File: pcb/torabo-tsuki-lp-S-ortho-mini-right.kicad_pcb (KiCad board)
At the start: 2 copper layers, 138.8 x 69 mm, 67 parts, among them J201 Conn_01x06_MountingPin, SW201 SW_SPDT, SW43 SW_Push, SW44 SW_Push, SW45 SW_Push, SW46 SW_Push, SW47 SW_Push, SW48 SW_Push, SW50 SW_Push, SW51 SW_Push, SW52 SW_Push, SW53 SW_Push, SW54 SW_Push, SW55 SW_Push, SW57 SW_Push, SW58 SW_Push, SW59 SW_Push, SW60 SW_Push, SW61 SW_Push, SW62 SW_Push, SW63 SW_Push, SW64 SW_Push, SW65 SW_Push, SW69 SW_Push, SW70 SW_Push, U201 XIAO nRF52840 Plus, U202 AE-XCL103-3V3, U203 XC8111AA01MR-G

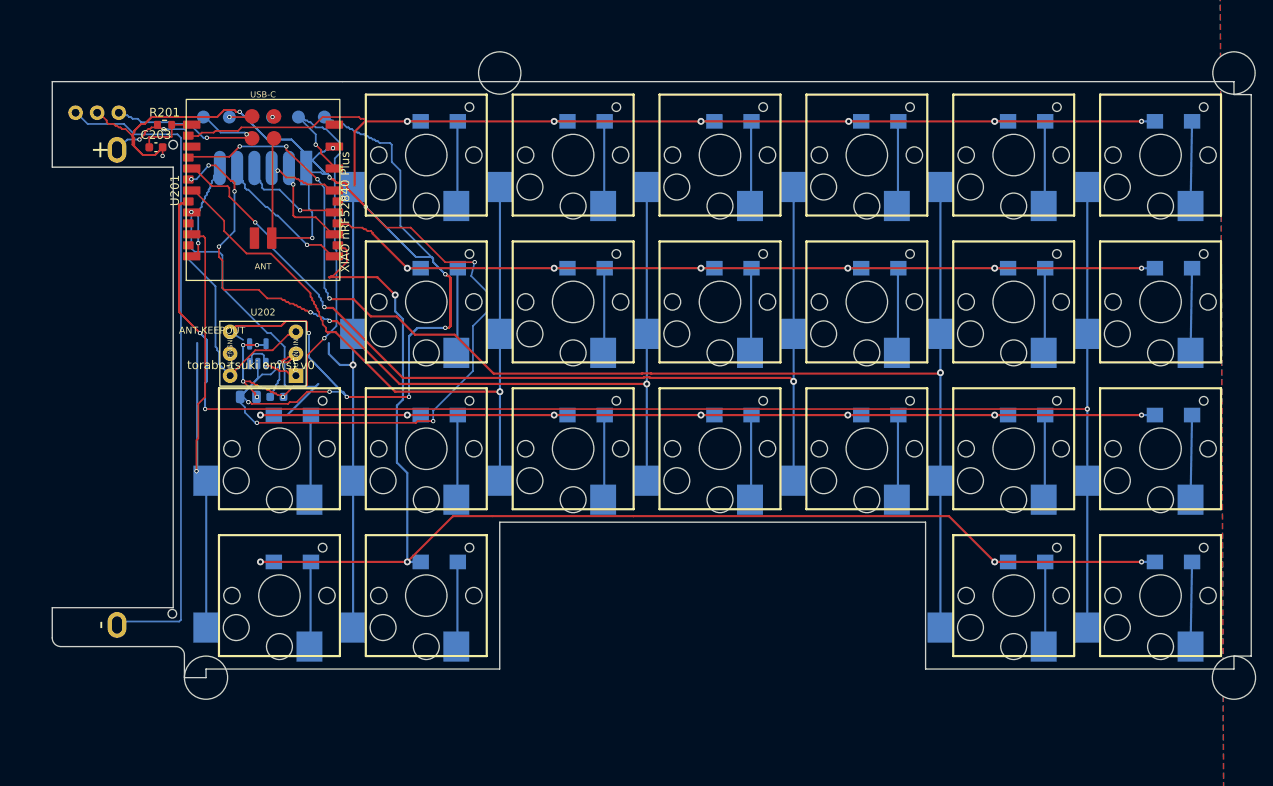
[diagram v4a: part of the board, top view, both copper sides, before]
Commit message: Convert split PCBs to column stagger
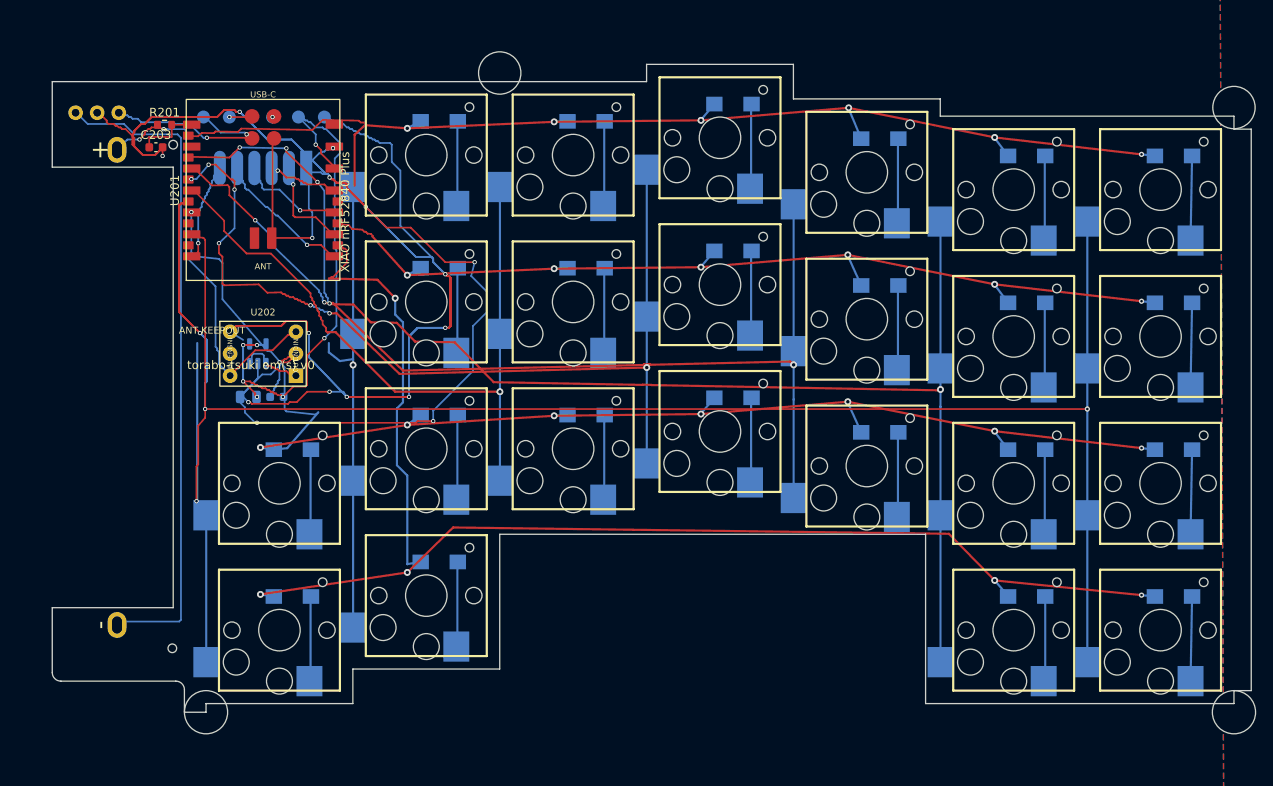
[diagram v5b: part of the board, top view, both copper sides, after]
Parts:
- moved D43 4.00 mm to (157.3, 126.1)
- moved D44 4.00 mm to (140.3, 126.1)
- moved D50 4.00 mm to (157.3, 143.1)
- moved D51 4.00 mm to (140.3, 143.1)
- moved D57 4.00 mm to (157.3, 160.1)
- moved D58 4.00 mm to (140.3, 160.1)
- moved D63 4.00 mm to (55.3, 160.1)
- moved D64 4.00 mm to (157.3, 177.1)
- moved D65 4.00 mm to (140.3, 177.1)
- moved D70 4.00 mm to (55.3, 177.1)
- moved REF** 4.00 mm to (164.3, 190.5)
- moved REF** 4.00 mm to (45.3, 190.5)
- moved REF** 4.00 mm to (164.3, 120.5)
- moved REF** 4.00 mm to (41.4, 183.1)
- moved SW43 4.00 mm to (155.8, 130.0)
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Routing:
- net /right/ROW3: track 150.0 -> 158.1 mm
- net /right/COL6: track 62.7 -> 69.9 mm
- net /right/ROW2: track 104.6 -> 110.1 mm
- net /right/ROW1: track 128.9 -> 133.7 mm
- net /right/ROW4: track 158.7 -> 160.0 mm
- net /right/COL3: track 108.0 -> 107.4 mm
- net /right/COL2: track 115.7 -> 115.2 mm
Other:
- board size 138.8 x 69 mm -> 138.8 x 75 mm

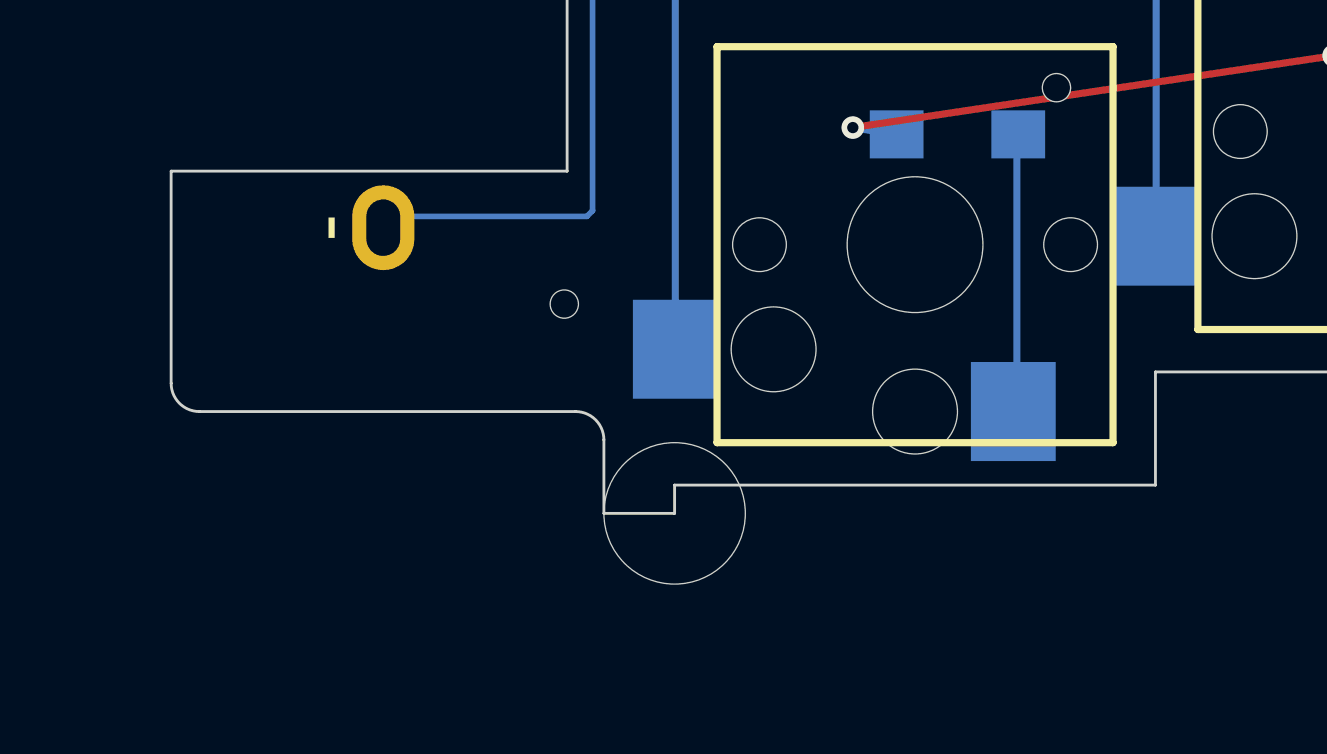
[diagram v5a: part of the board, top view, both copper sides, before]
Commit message: Refine staggered PCB outlines and mounting clearances
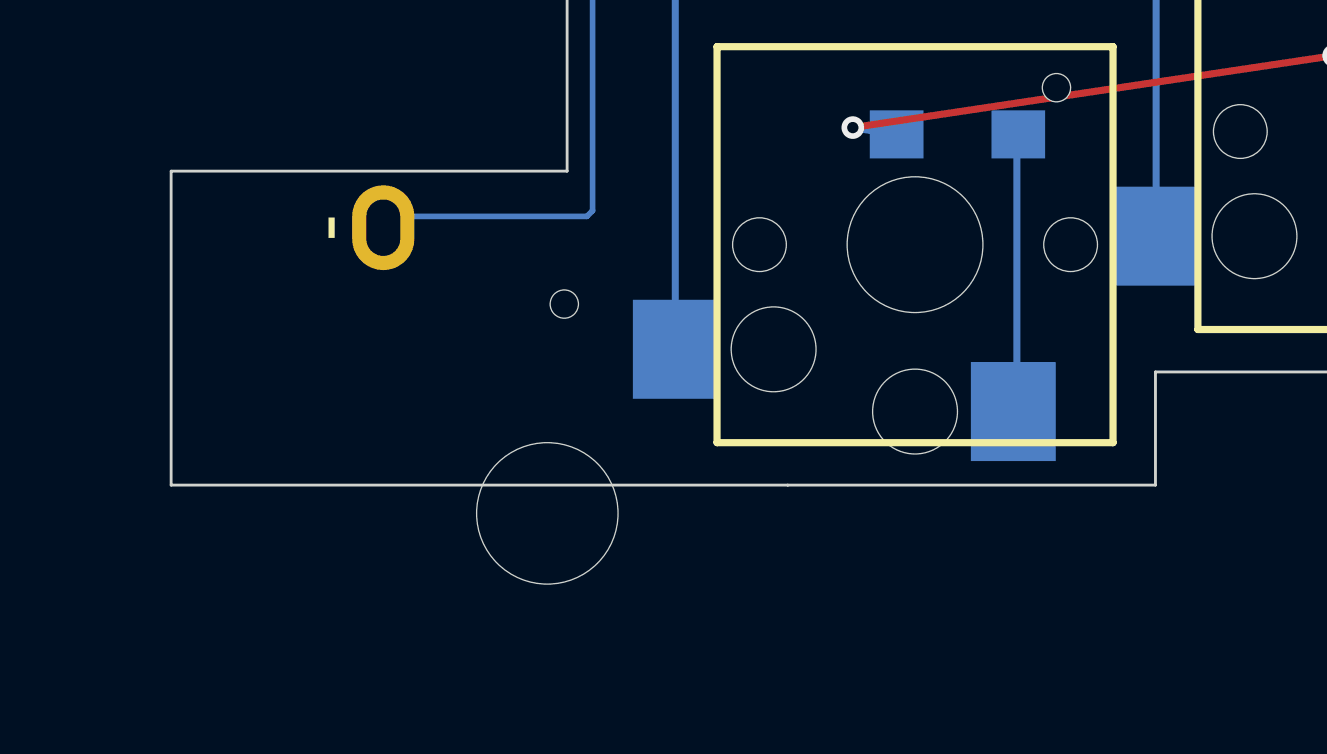
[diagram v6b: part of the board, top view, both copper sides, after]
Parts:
- moved REF** 4.50 mm to (40.8, 190.5)
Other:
- board size 138.8 x 75 mm -> 138.8 x 74 mm
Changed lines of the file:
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@@
 	(footprint "Library:MountingHole_5mm"
 		(layer "F.Cu")
-		(at 45.3 190.5)
+		(at 40.8 190.5)
 		(descr "Mounting Hole 5mm, no annular")
 		(tags "mounting hole 5mm no annular")
@@
 	)
 	(gr_line
-		(start 27.5 185.9)
+		(start 27.5 189.5)
 		(end 27.5 178.4)
 		(stroke
@@
 		(layer "Edge.Cuts")
 	)
-	(gr_arc
-		(start 28.5 186.9)
-		(mid 27.792893 186.607107)
-		(end 27.5 185.9)
-		(stroke
-			(width 0.1)
-			(type default)
-		)
-		(layer "Edge.Cuts")
-	)
 	(gr_line
 		(start 41.5 127.4)
@@
 	)
 	(gr_line
-		(start 41.8 186.9)
-		(end 28.5 186.9)
-		(stroke
-			(width 0.1)
-			(type default)
-		)
-		(layer "Edge.Cuts")
-	)
-	(gr_arc
-		(start 41.8 186.9)
-		(mid 42.507107 187.192893)
-		(end 42.8 187.9)
-		(stroke
-			(width 0.1)
-			(type default)
-		)
-		(layer "Edge.Cuts")
-	)
-	(gr_line
-		(start 42.8 190.5)
-		(end 42.8 187.9)
-		(stroke
-			(width 0.1)
-			(type default)
-		)
-		(layer "Edge.Cuts")
-	)
-	(gr_line
-		(start 45.3 189.5)
-		(end 45.3 190.5)
-		(stroke
-			(width 0.1)
-			(type default)
-		)
-		(layer "Edge.Cuts")
-	)
-	(gr_line
-		(start 45.3 190.5)
-		(end 42.8 190.5)
+		(start 49.3 189.5)
+		(end 27.5 189.5)
 		(stroke
 			(width 0.1)
@@
 	(gr_line
 		(start 62.3 189.5)
-		(end 45.3 189.5)
+		(end 49.3 189.5)
 		(stroke
 			(width 0.1)
@@
 		(layer "B.Cu")
 		(hatch none 0.1)
-		(priority 30137)
+		(priority 30138)
 		(attr
 			(teardrop
@@
 		(polygon
 			(pts
-				(xy 79.45 152.603422) (xy 79.2 152.603422) (xy 78.955448 153.246927) (xy 79.325 153.404422) (xy 79.694552 153.246927)
+				(xy 79.2 154.196578) (xy 79.45 154.196578) (xy 79.694552 153.553073) (xy 79.325 153.395578) (xy 78.955448 153.553073)
 			)
 		)
@@
 		(layer "B.Cu")
 		(hatch none 0.1)
-		(priority 30030)
+		(priority 30035)
 		(attr
 			(teardrop
@@
 		(polygon
 			(pts
-				(xy 79.45 143.95) (xy 79.2 143.95) (xy 78.325 144.95) (xy 79.325 146.701) (xy 80.325 144.95)
+				(xy 79.45 160.95) (xy 79.2 160.95) (xy 78.325 161.95) (xy 79.325 163.701) (xy 80.325 161.95)
 			)
 		)
 	)
 	(zone
-		(net "Net-(D54-K)")
+		(net "Net-(D61-K)")
 		(layer "B.Cu")
 		(hatch none 0.1)
-		(priority 30073)
+		(priority 30045)
 		(attr
 			(teardrop
@@
 		(polygon
 			(pts
-				(xy 91.275 140.8005) (xy 91.525 140.8005) (xy 92.25 139.9505) (xy 91.4 139.0995) (xy 90.55 139.9505)
+				(xy 91.525 163.15) (xy 91.275 163.15) (xy 90.4 164.15) (xy 91.4 165.901) (xy 92.4 164.15)
 			)
 		)
 	)
 	(zone
-		(net "/right/COL4")
+		(net "Net-(BT201--)")
 		(layer "B.Cu")
 		(hatch none 0.1)
-		(priority 30033)
+		(priority 30055)
 		(attr
 			(teardrop
@@
 		(polygon
 			(pts
-				(xy 79.2 149.45) (xy 79.45 149.45) (xy 80.325 148.45) (xy 79.325 146.699) (xy 78.325 148.45)
+				(xy 37.1 177.925) (xy 37.1 177.675) (xy 35.919558 176.8) (xy 34.999 177.8) (xy 35.919558 178.8)
 			)
 		)
 	)
 	(zone
-		(net "Net-(BT201--)")
+		(net "Net-(D47-K)")
 		(layer "B.Cu")
 		(hatch none 0.1)
-		(priority 30055)
+		(priority 30037)
 		(attr
 			(teardrop
@@
 		(polygon
 			(pts
-				(xy 37.1 177.925) (xy 37.1 177.675) (xy 35.919558 176.8) (xy 34.999 177.8) (xy 35.919558 178.8)
+				(xy 91.525 129.15) (xy 91.275 129.15) (xy 90.4 130.15) (xy 91.4 131.901) (xy 92.4 130.15)
 			)
 		)
 	)
 	(zone
-		(net "Net-(BT201--)")
+		(net "/right/COL4")
 		(layer "B.Cu")
 		(hatch none 0.1)
-		(priority 30081)
+		(priority 30137)
 		(attr
 			(teardrop
@@
 		(polygon
 			(pts
-				(xy 30.3 116.804093) (xy 30.1 116.804093) (xy 29.450367 118.099313) (xy 30.2 118.505093) (xy 30.949633 118.099313)
+				(xy 79.45 152.603422) (xy 79.2 152.603422) (xy 78.955448 153.246927) (xy 79.325 153.404422) (xy 79.694552 153.246927)
 			)
 		)
@@
 		(layer "B.Cu")
 		(hatch none 0.1)
-		(priority 30138)
+		(priority 30033)
 		(attr
 			(teardrop
@@
 		(polygon
 			(pts
-				(xy 79.2 154.196578) (xy 79.45 154.196578) (xy 79.694552 153.553073) (xy 79.325 153.395578) (xy 78.955448 153.553073)
+				(xy 79.2 149.45) (xy 79.45 149.45) (xy 80.325 148.45) (xy 79.325 146.699) (xy 78.325 148.45)
 			)
 		)
 	)
 	(zone
-		(net "Net-(D47-K)")
+		(net "/right/COL4")
 		(layer "B.Cu")
 		(hatch none 0.1)
-		(priority 30076)
+		(priority 30030)
 		(attr
 			(teardrop
@@
 		(polygon
 			(pts
-				(xy 91.275 123.8005) (xy 91.525 123.8005) (xy 92.25 122.9505) (xy 91.4 122.0995) (xy 90.55 122.9505)
+				(xy 79.45 143.95) (xy 79.2 143.95) (xy 78.325 144.95) (xy 79.325 146.701) (xy 80.325 144.95)
 			)
 		)
 	)
 	(zone
-		(net "/right/COL4")
+		(net "Net-(D54-K)")
 		(layer "B.Cu")
 		(hatch none 0.1)
-		(priority 30035)
+		(priority 30073)
 		(attr
 			(teardrop
@@
 		(polygon
 			(pts
-				(xy 79.45 160.95) (xy 79.2 160.95) (xy 78.325 161.95) (xy 79.325 163.701) (xy 80.325 161.95)
+				(xy 91.275 140.8005) (xy 91.525 140.8005) (xy 92.25 139.9505) (xy 91.4 139.0995) (xy 90.55 139.9505)
 			)
 		)
 	)
 	(zone
-		(net "Net-(D61-K)")
+		(net "Net-(BT201--)")
 		(layer "B.Cu")
 		(hatch none 0.1)
-		(priority 30045)
+		(priority 30081)
 		(attr
 			(teardrop
@@
 		(polygon
 			(pts
-				(xy 91.525 163.15) (xy 91.275 163.15) (xy 90.4 164.15) (xy 91.4 165.901) (xy 92.4 164.15)
+				(xy 30.3 116.804093) (xy 30.1 116.804093) (xy 29.450367 118.099313) (xy 30.2 118.505093) (xy 30.949633 118.099313)
 			)
 		)
 	)
 	(zone
-		(net "Net-(D61-K)")
+		(net "/right/COL4")
 		(layer "B.Cu")
 		(hatch none 0.1)
-		(priority 30069)
+		(priority 30031)
 		(attr
 			(teardrop
@@
 		(polygon
 			(pts
-				(xy 91.275 157.8005) (xy 91.525 157.8005) (xy 92.25 156.9505) (xy 91.4 156.0995) (xy 90.55 156.9505)
+				(xy 79.2 132.45) (xy 79.45 132.45) (xy 80.325 131.45) (xy 79.325 129.699) (xy 78.325 131.45)
 			)
 		)
 	)
 	(zone
-		(net "Net-(D47-K)")
+		(net "Net-(D61-K)")
 		(layer "B.Cu")
 		(hatch none 0.1)
-		(priority 30037)
+		(priority 30069)
 		(attr
 			(teardrop
@@
 		(polygon
 			(pts
-				(xy 91.525 129.15) (xy 91.275 129.15) (xy 90.4 130.15) (xy 91.4 131.901) (xy 92.4 130.15)
+				(xy 91.275 157.8005) (xy 91.525 157.8005) (xy 92.25 156.9505) (xy 91.4 156.0995) (xy 90.55 156.9505)
 			)
 		)
 	)
 	(zone
-		(net "/right/COL4")
+		(net "Net-(D47-K)")
 		(layer "B.Cu")
 		(hatch none 0.1)
-		(priority 30031)
+		(priority 30076)
 		(attr
 			(teardrop
@@
 		(polygon
 			(pts
-				(xy 79.2 132.45) (xy 79.45 132.45) (xy 80.325 131.45) (xy 79.325 129.699) (xy 78.325 131.45)
+				(xy 91.275 123.8005) (xy 91.525 123.8005) (xy 92.25 122.9505) (xy 91.4 122.0995) (xy 90.55 122.9505)
 			)
 		)
